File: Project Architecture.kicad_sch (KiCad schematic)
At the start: 18 parts, among them J1 SM06B-SRSS-TB_LF__SN_, J2 SM06B-SRSS-TB_LF__SN_, J3 UJ20-C-H-G-SMT-1-P16-TR, J4 SM08B-SRSS-TB(LF)(SN), Q2 SS8050

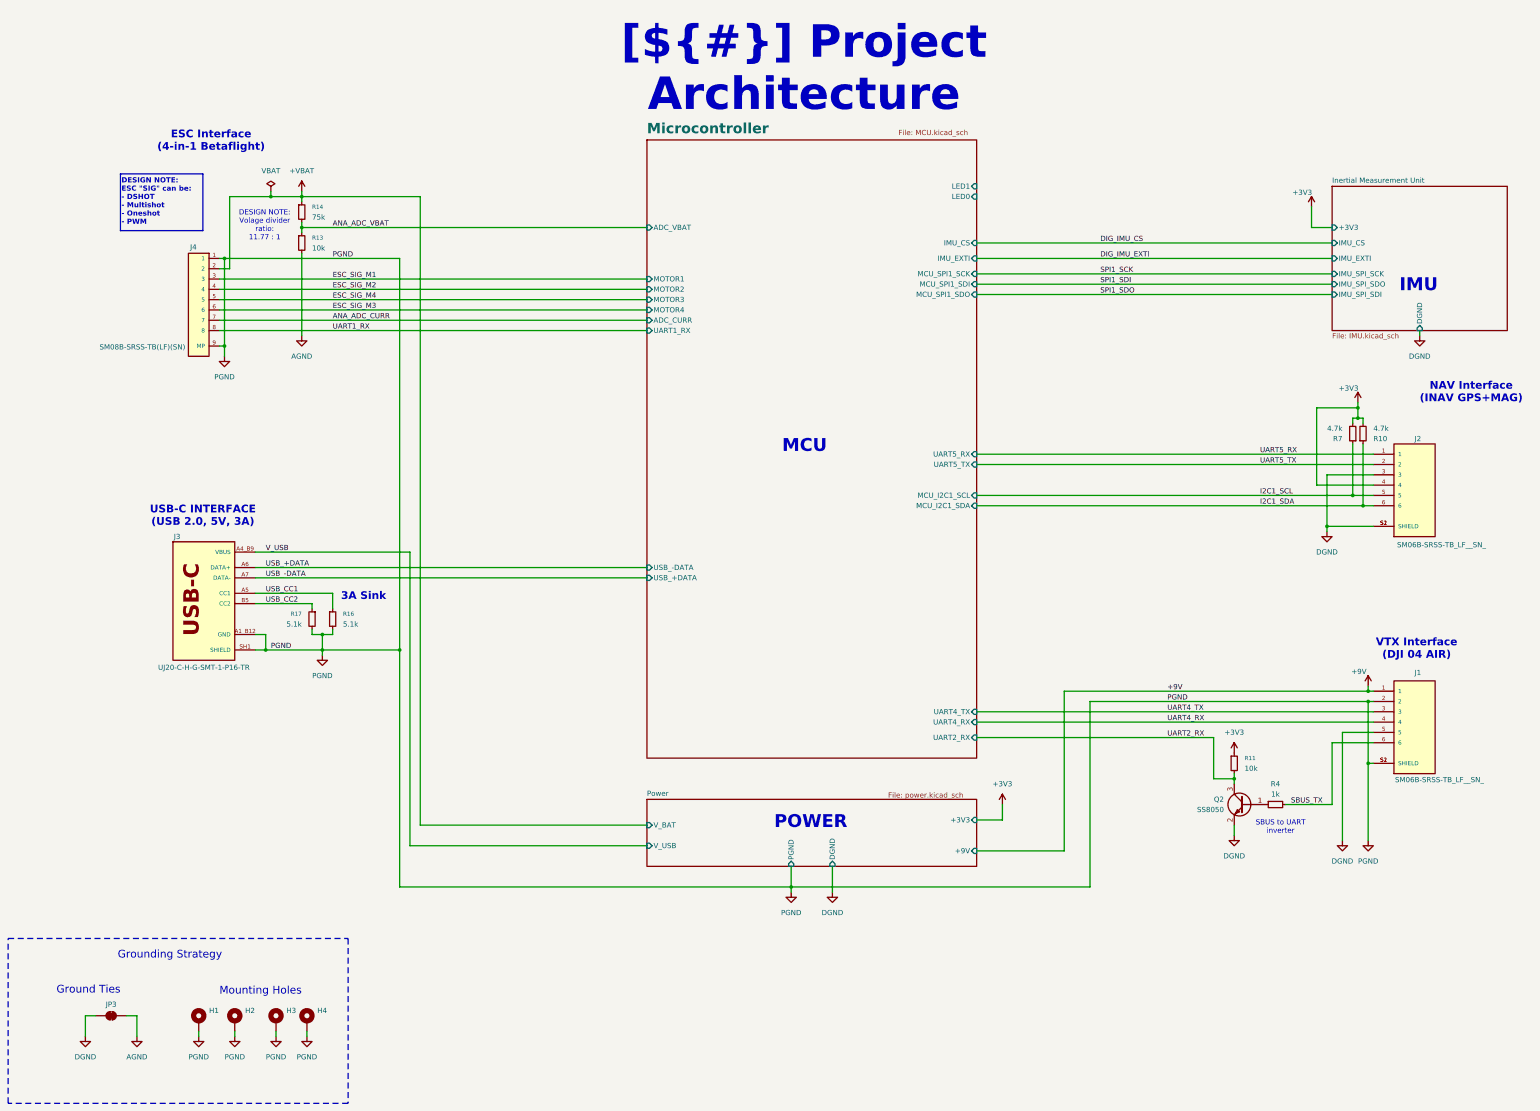
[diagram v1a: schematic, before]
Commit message: More symbols updated to be compliant
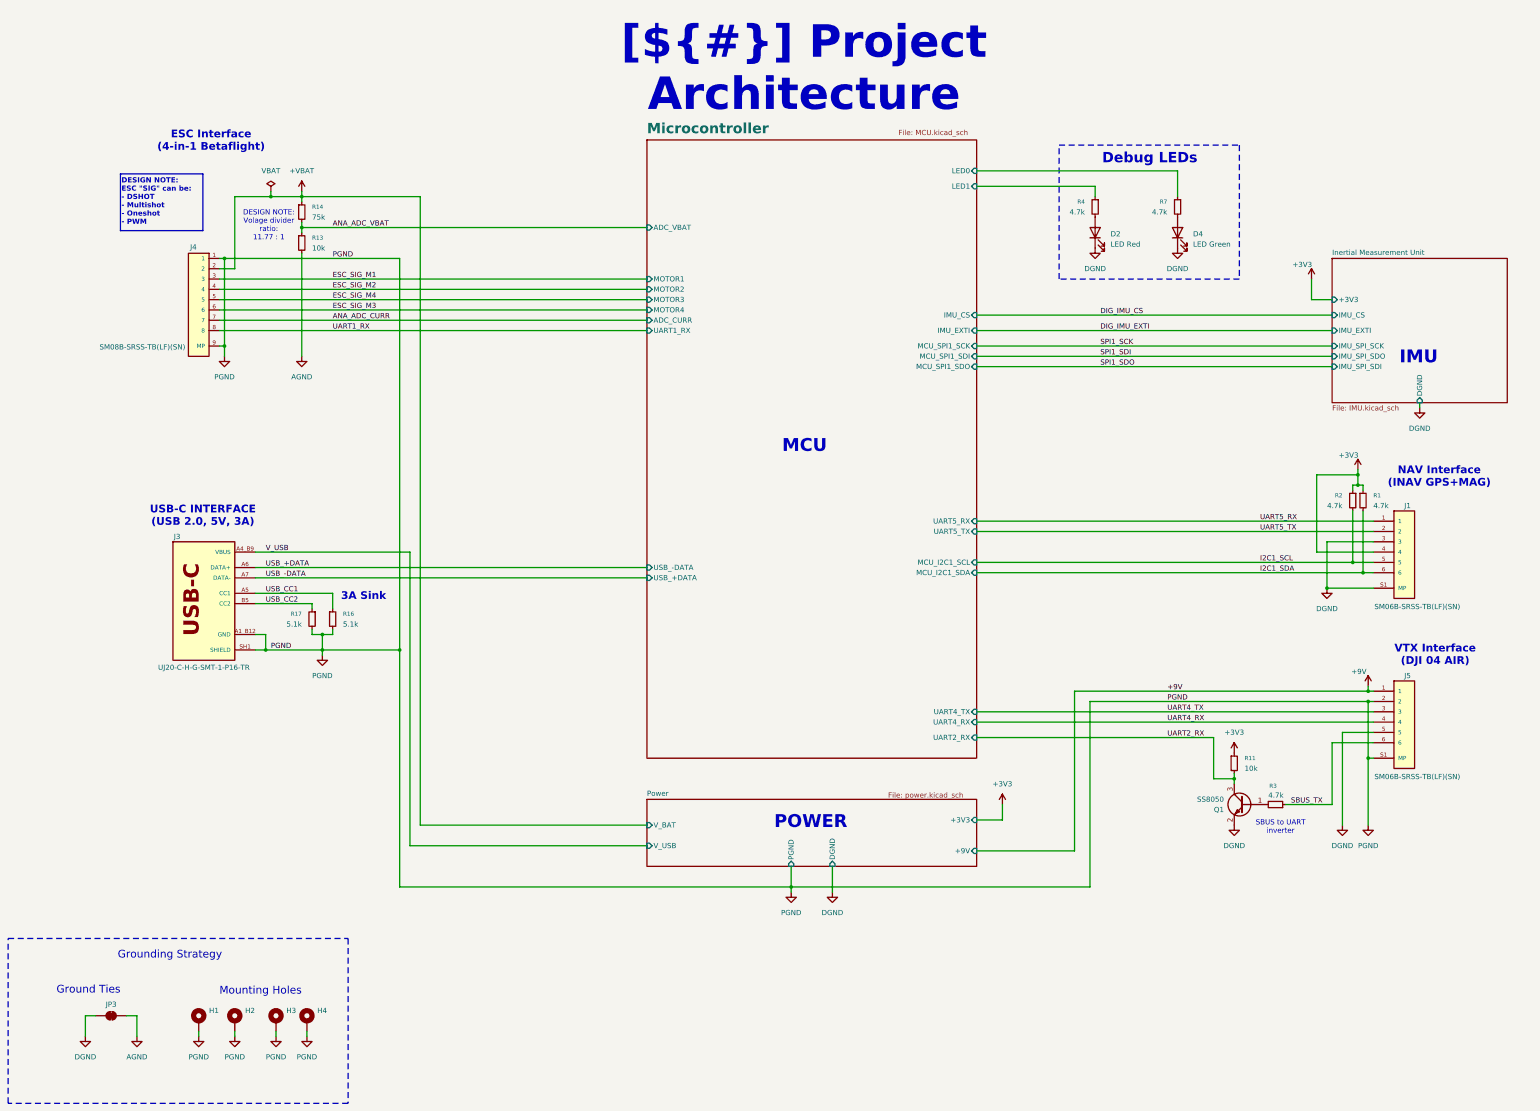
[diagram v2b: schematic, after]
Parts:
- removed J1, J2: SM06B-SRSS-TB_LF__SN_, KSE_connector:JST_SM06B-SRSS-TB_LF__SN_, symbol KSE_connectors:SM06B-SRSS-TB_LF__SN_
- removed Q2: SS8050, Package_TO_SOT_SMD:SOT-23, symbol Transistor_BJT:SS8050
- removed R10, R7: 4.7k, Resistor_SMD:R_0603_1608Metric_Pad0.98x0.95mm_HandSolder, symbol Device:R_Small
- removed R4: 1k, Resistor_SMD:R_0603_1608Metric_Pad0.98x0.95mm_HandSolder, symbol Device:R_Small
- added D2: LED Red, Diode_SMD:D_0603_1608Metric, symbol KSE_Diodes:LED
- added D4: LED Green, Diode_SMD:D_0603_1608Metric, symbol KSE_Diodes:LED
- added J1, J5: SM06B-SRSS-TB(LF)(SN), KSE_connector:JST_SM06B-SRSS-TB(LF)(SN), symbol KSE_connectors:SM06B-SRSS-TB(LF)(SN)
- added Q1: SS8050, Package_TO_SOT_SMD:SOT-23, symbol KSE_Transistors:SS8050
- added R1, R2, R3, R4, R7: 4.7k, Resistor_SMD:R_0402_1005Metric, symbol KSE_Resistors:R_Small
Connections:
- net +3V3: now also J1.4, R1.1, R2.1
- net +9V: now also J5.1
- net DGND: now also D2.1 (K), D4.1 (K), J1.3, J1.S1 (MP), J1.S2 (MP), J5.5, Q1.2 (E)
- net I2C1_SCL: now also J1.5, R2.2
- net I2C1_SDA: now also J1.6, R1.2
- net Microcontroller/LED0: now also R7.1
- net Microcontroller/LED1: now also R4.1
- net PGND: now also J5.2, J5.S1 (MP), J5.S2 (MP)
- net SBUS_TX: now also J5.6, R3.1
- net UART2_RX: now also Q1.3 (C)
- net UART4_RX: now also J5.4
- net UART4_TX: now also J5.3
- net UART5_RX: now also J1.1
- net UART5_TX: now also J1.2
- new net: D2.2 (A), R4.2
- new net: Q1.1 (B), R3.2
- new net: D4.2 (A), R7.2
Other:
- note added: "Debug LEDs"

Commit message: Layout Draft Complete
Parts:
- J4: footprint KSE_connector:JST_SM08B-SRSS-TB_LF__SN_ -> KSE_connector:JST_SM08B-SRSS-TB(LF)(SN)
- R4, R7: value 4.7k -> 680; MPN RCG04024K70JNED -> RE0402FRE07680RL; Manufacturer Vishay / Draloric -> YAGEO
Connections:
- net DGND: no longer J1.S1 (MP), J1.S2 (MP)
- net PGND: now also J1.S1 (MP), J1.S2 (MP)

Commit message: Finished DRC/ERC
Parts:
- J4: footprint KSE_connector:JST_SM08B-SRSS-TB(LF)(SN) -> KSE_connector:JST_SM08B-SRSS-TB_LF__SN_
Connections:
- net PGND: now also J1.MP, J4.MP, J5.MP; no longer J1.S1 (MP), J1.S2 (MP), J4.9 (MP), J5.S1 (MP), J5.S2 (MP)
- net at J3.A8 (SBU1): no longer J3.B8 (SBU2)
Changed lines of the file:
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@@
 	(text "Ground Ties"
 		(exclude_from_sim no)
-		(at 33.782 255.27 0)
+		(at 34.036 252.73 0)
 		(effects
 			(font
@@
 	)
 	(junction
+		(at 45.72 261.62)
+		(diameter 0)
+		(color 0 0 0 0)
+	)
+	(junction
 		(at 69.85 266.7)
 		(diameter 0)
@@
 	)
 	(junction
+		(at 33.02 261.62)
+		(diameter 0)
+		(color 0 0 0 0)
+	)
+	(junction
 		(at 349.25 184.15)
 		(diameter 0)
@@
 	)
 	(symbol
+		(lib_id "power:PWR_FLAG")
+		(at 33.02 261.62 0)
+		(unit 1)
+		(exclude_from_sim no)
+		(in_bom yes)
+		(on_board yes)
+		(dnp no)
+		(fields_autoplaced yes)
+		(property "Reference" "#FLG03"
+			(at 33.02 259.715 0)
+			(effects
+				(font
+					(size 1.27 1.27)
+				)
+				(hide yes)
+			)
+		)
+		(property "Value" "DGND"
+			(at 33.02 256.54 0)
+			(effects
+				(font
+					(size 1.27 1.27)
+				)
+			)
+		)
+		(property "Footprint" ""
+			(at 33.02 261.62 0)
+			(effects
+				(font
+					(size 1.27 1.27)
+				)
+				(hide yes)
+			)
+		)
+		(property "Datasheet" "~"
+			(at 33.02 261.62 0)
+			(effects
+				(font
+					(size 1.27 1.27)
+				)
+				(hide yes)
+			)
+		)
+		(property "Description" "Special symbol for telling ERC where power comes from"
+			(at 33.02 261.62 0)
+			(effects
+				(font
+					(size 1.27 1.27)
+				)
+				(hide yes)
+			)
+		)
+		(pin "1"
+		)
+		(instances
+			(project "FCU3"
+				(path "/f9e05184-c88b-4a88-ae9c-ab2bdb32be7c/c5103ceb-5325-4a84-a025-9638a412984e"
+					(reference "#FLG03")
+					(unit 1)
+				)
+			)
+		)
+	)
+	(symbol
 		(lib_id "KSE_Diodes:LED")
 		(at 281.94 68.58 90)
@@
 	)
 	(symbol
+		(lib_name "SM06B-SRSS-TB(LF)(SN)_1")
 		(lib_id "KSE_connectors:SM06B-SRSS-TB(LF)(SN)")
 		(at 358.14 187.96 0)
@@
 		(pin "3"
 		)
-		(pin "S1"
+		(pin "MP"
 		)
 		(pin "4"
@@
 		(pin "5"
 		)
-		(pin "S2"
-		)
 		(pin "1"
 		)
@@
 		(pin "3"
 		)
-		(pin "S1"
+		(pin "MP"
 		)
 		(pin "4"
@@
 		(pin "5"
 		)
-		(pin "S2"
-		)
 		(pin "1"
 		)
@@
 			)
 		)
-		(property "Footprint" "KSE_connector:JST_SM08B-SRSS-TB(LF)(SN)"
+		(property "Footprint" "KSE_connector:JST_SM08B-SRSS-TB_LF__SN_"
 			(at 60.706 106.172 0)
 			(effects
@@
 		(pin "2"
 		)
-		(pin "9"
+		(pin "MP"
 		)
 		(instances
@@
 	)
 	(symbol
+		(lib_id "power:PWR_FLAG")
+		(at 45.72 261.62 0)
+		(unit 1)
+		(exclude_from_sim no)
+		(in_bom yes)
+		(on_board yes)
+		(dnp no)
+		(fields_autoplaced yes)
+		(property "Reference" "#FLG02"
+			(at 45.72 259.715 0)
+			(effects
+				(font
+					(size 1.27 1.27)
+				)
+				(hide yes)
+			)
+		)
+		(property "Value" "AGND"
+			(at 45.72 256.54 0)
+			(effects
+				(font
+					(size 1.27 1.27)
+				)
+			)
+		)
+		(property "Footprint" ""
+			(at 45.72 261.62 0)
+			(effects
+				(font
+					(size 1.27 1.27)
+				)
+				(hide yes)
+			)
+		)
+		(property "Datasheet" "~"
+			(at 45.72 261.62 0)
+			(effects
+				(font
+					(size 1.27 1.27)
+				)
+				(hide yes)
+			)
+		)
+		(property "Description" "Special symbol for telling ERC where power comes from"
+			(at 45.72 261.62 0)
+			(effects
+				(font
+					(size 1.27 1.27)
+				)
+				(hide yes)
+			)
+		)
+		(pin "1"
+		)
+		(instances
+			(project ""
+				(path "/f9e05184-c88b-4a88-ae9c-ab2bdb32be7c/c5103ceb-5325-4a84-a025-9638a412984e"
+					(reference "#FLG02")
+					(unit 1)
+				)
+			)
+		)
+	)
+	(symbol
 		(lib_id "power:+3.3V")
 		(at 346.71 127 0)
@@
 			)
 		)
-		(pin "V_BAT" input
-			(at 171.45 214.63 180)
-			(effects
-				(font
-					(size 1.27 1.27)
-				)
-				(justify left)
-			)
-		)
 		(pin "V_USB" input
 			(at 171.45 219.71 180)
@@
 			(effects
 				(font
+					(size 1.27 1.27)
+				)
+				(justify left)
+			)
+		)
+		(pin "V_BAT" input
+			(at 171.45 214.63 180)
+			(effects
+				(font

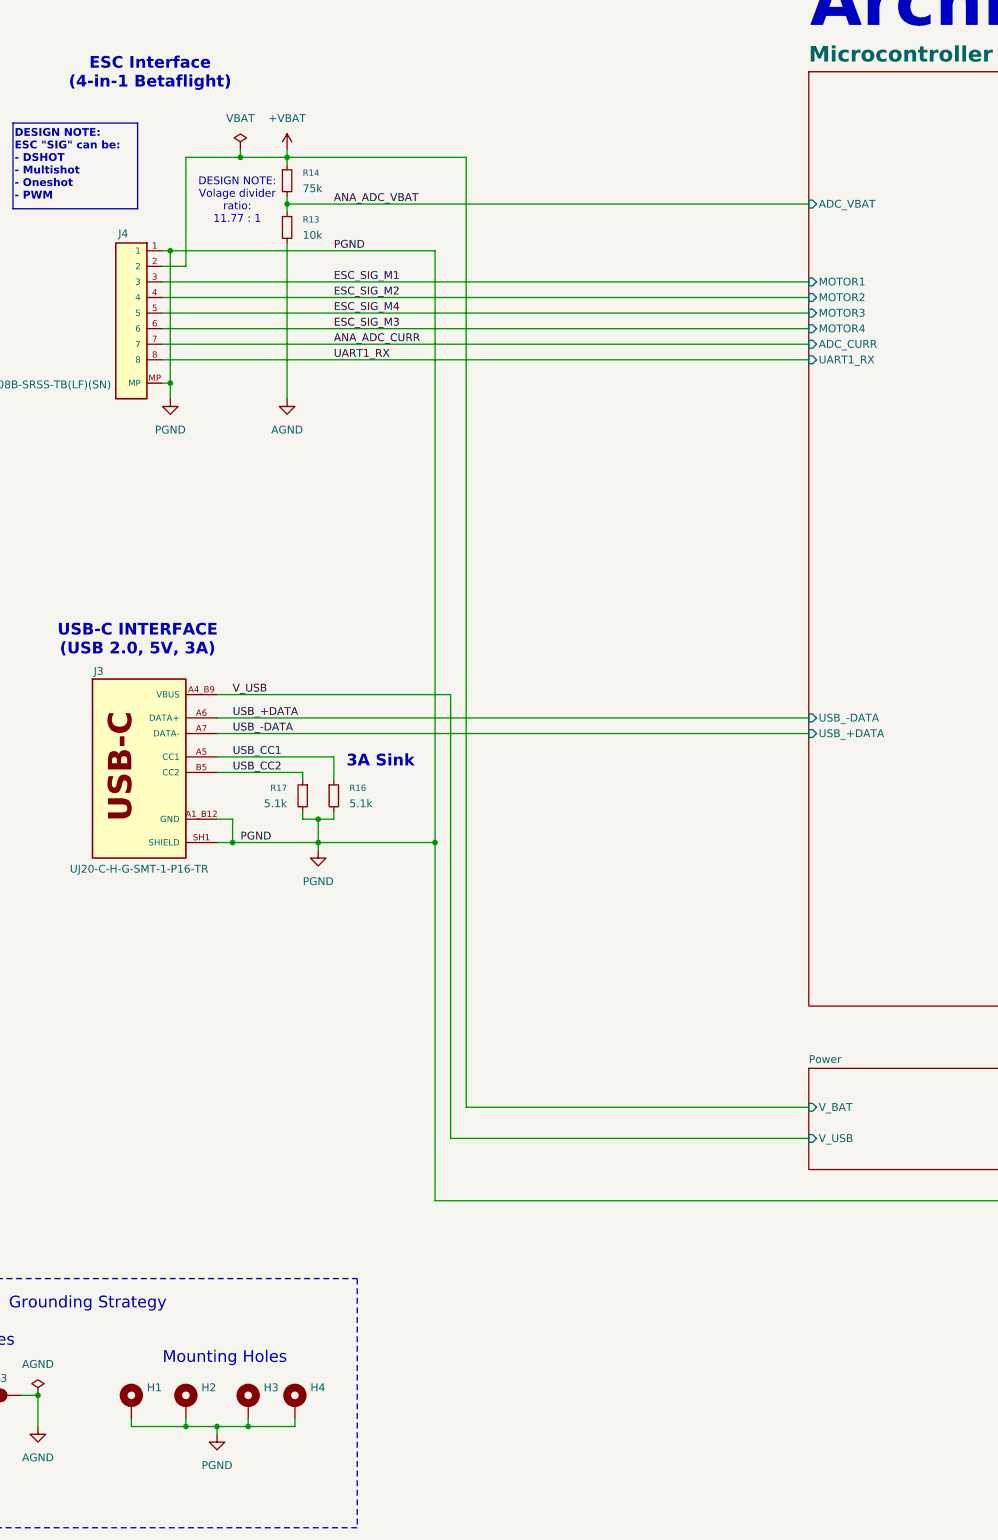
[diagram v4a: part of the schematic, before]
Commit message: Fixed ESC connector pinout
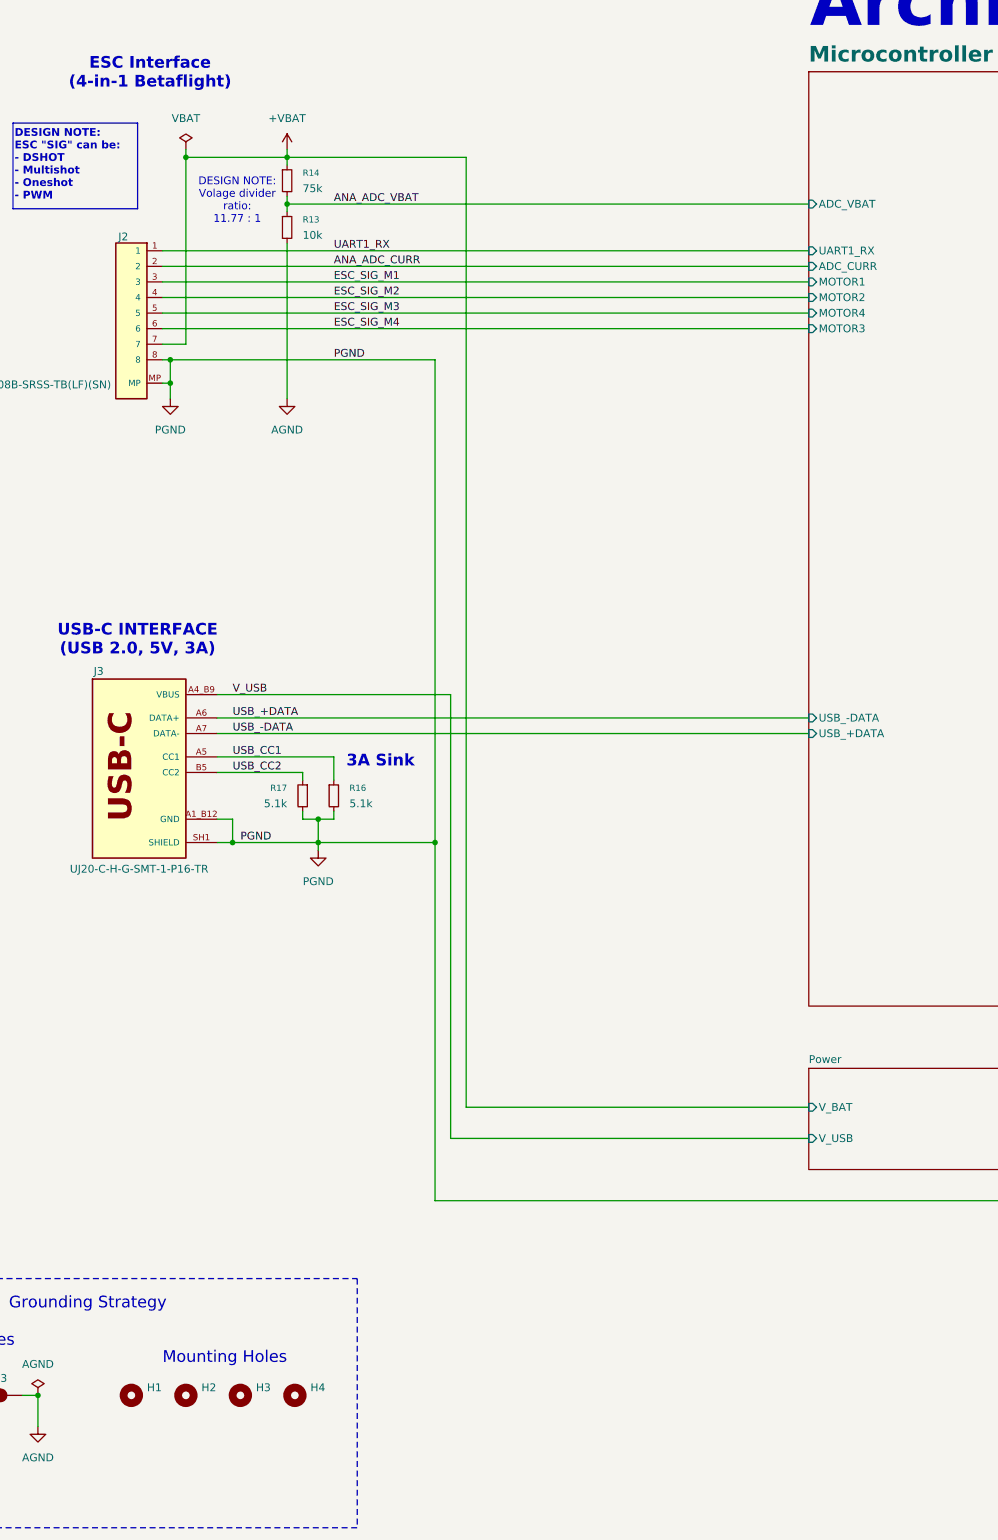
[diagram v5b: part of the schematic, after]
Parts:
- removed H1, H2, H3, H4: MountingHole_Pad_MP, MountingHole:MountingHole_3.2mm_M3_DIN965_Pad, symbol Mechanical:MountingHole_Pad_MP
- removed J4: SM08B-SRSS-TB(LF)(SN), KSE_connector:JST_SM08B-SRSS-TB_LF__SN_, symbol KSE_connectors:SM08B-SRSS-TB(LF)(SN)
- added H1, H2, H3, H4: MountingHole, MountingHole:MountingHole_3.2mm_M3_ISO7380, symbol Mechanical:MountingHole
- added J2: SM08B-SRSS-TB(LF)(SN), KSE_connector:JST_SM08B-SRSS-TB(LF)(SN), symbol KSE_connectors:SM08B-SRSS-TB(LF)(SN)
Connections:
- net +VBAT: now also J2.7
- net ANA_ADC_CURR: now also J2.2
- net ESC_SIG_M1: now also J2.3
- net ESC_SIG_M2: now also J2.4
- net ESC_SIG_M3: now also J2.5
- net ESC_SIG_M4: now also J2.6
- net PGND: now also J2.8, J2.MP
- net UART1_RX: now also J2.1
